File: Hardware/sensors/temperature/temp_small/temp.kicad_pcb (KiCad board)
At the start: 2 copper layers, 20.6 x 4.6 mm, 7 parts, among them J1 Conn_01x01, J2 Conn_01x01, J3 Conn_01x01, J4 Conn_01x01, J5 Conn_01x01, J6 Conn_01x01, U1 TMP1826DGK

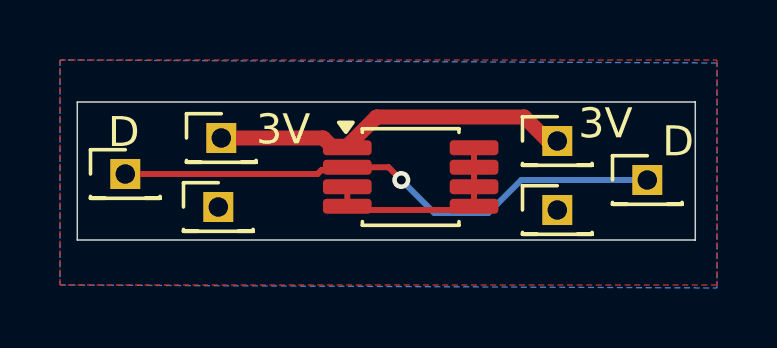
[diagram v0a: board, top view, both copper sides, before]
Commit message: Added PAR sensor PCB
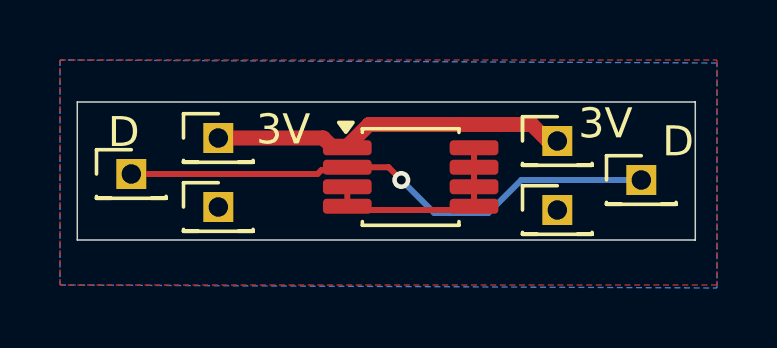
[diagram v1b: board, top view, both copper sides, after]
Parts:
- moved J3 0.20 mm to (125.5, 81.5)
- moved J5 0.20 mm to (142.5, 81.7)
- moved J4 0.10 mm to (128.4, 80.3)
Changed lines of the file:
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@@
 		)
 		(property "Value" "TMP1826DGK"
-			(at 0 2.45 0)
+			(at 0 3.1 0)
 			(layer "F.Fab")
 			(effects
@@
 	(footprint "Connector_PinHeader_1.27mm:PinHeader_1x01_P1.27mm_Vertical"
 		(layer "F.Cu")
-		(at 128.5 80.3)
+		(at 128.4 80.3)
 		(descr "Through hole straight pin header, 1x01, 1.27mm pitch, single row")
 		(tags "Through hole pin header THT 1x01 1.27mm single row")
@@
 			(at 0 1.745 0)
 			(layer "F.Fab")
+			(hide yes)
 			(effects
 				(font
@@
 			(at 0 1.745 0)
 			(layer "F.Fab")
+			(hide yes)
 			(effects
 				(font
@@
 	(footprint "Connector_PinHeader_1.27mm:PinHeader_1x01_P1.27mm_Vertical"
 		(layer "F.Cu")
-		(at 125.3 81.5)
+		(at 125.5 81.5)
 		(descr "Through hole straight pin header, 1x01, 1.27mm pitch, single row")
 		(tags "Through hole pin header THT 1x01 1.27mm single row")
@@
 			(at 0 1.745 0)
 			(layer "F.Fab")
+			(hide yes)
 			(effects
 				(font
@@
 			(at 0 1.745 0)
 			(layer "F.Fab")
+			(hide yes)
 			(effects
 				(font
@@
 	(footprint "Connector_PinHeader_1.27mm:PinHeader_1x01_P1.27mm_Vertical"
 		(layer "F.Cu")
-		(at 142.7 81.7)
+		(at 142.5 81.7)
 		(descr "Through hole straight pin header, 1x01, 1.27mm pitch, single row")
 		(tags "Through hole pin header THT 1x01 1.27mm single row")
@@
 			(at 0 1.745 0)
 			(layer "F.Fab")
+			(hide yes)
 			(effects
 				(font
@@
 			(at 0 1.745 0)
 			(layer "F.Fab")
+			(hide yes)
 			(effects
 				(font
@@
 	)
 	(segment
-		(start 139.4 80.4)
-		(end 138.6 79.6)
+		(start 139.7 80.4)
+		(end 139.4 80.4)
 		(width 0.5)
 		(layer "F.Cu")
@@
 	)
 	(segment
-		(start 138.6 79.6)
-		(end 133.675 79.6)
+		(start 132.7 80.575)
+		(end 132.175 80.575)
+		(width 0.5)
+		(layer "F.Cu")
+		(net 2)
+	)
+	(segment
+		(start 132.175 80.575)
+		(end 131.9 80.3)
+		(width 0.5)
+		(layer "F.Cu")
+		(net 2)
+	)
+	(segment
+		(start 133.425 79.85)
+		(end 132.7 80.575)
 		(width 0.5)
 		(layer "F.Cu")
@@
 	)
 	(segment
-		(start 133.675 79.6)
-		(end 132.7 80.575)
+		(start 138.85 79.85)
+		(end 133.425 79.85)
 		(width 0.5)
 		(layer "F.Cu")
@@
 	)
 	(segment
-		(start 139.7 80.4)
-		(end 139.4 80.4)
+		(start 139.4 80.4)
+		(end 138.85 79.85)
 		(width 0.5)
 		(layer "F.Cu")
-		(net 2)
-	)
-	(segment
-		(start 132.7 80.575)
-		(end 132.175 80.575)
-		(width 0.5)
-		(layer "F.Cu")
-		(net 2)
-	)
-	(segment
-		(start 132.175 80.575)
-		(end 131.9 80.3)
-		(width 0.5)
-		(layer "F.Cu")
